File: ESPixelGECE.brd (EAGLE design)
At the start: 35.1 x 46 mm, 15 parts, among them Q1 MOSFET-NCHANNEL2N7000

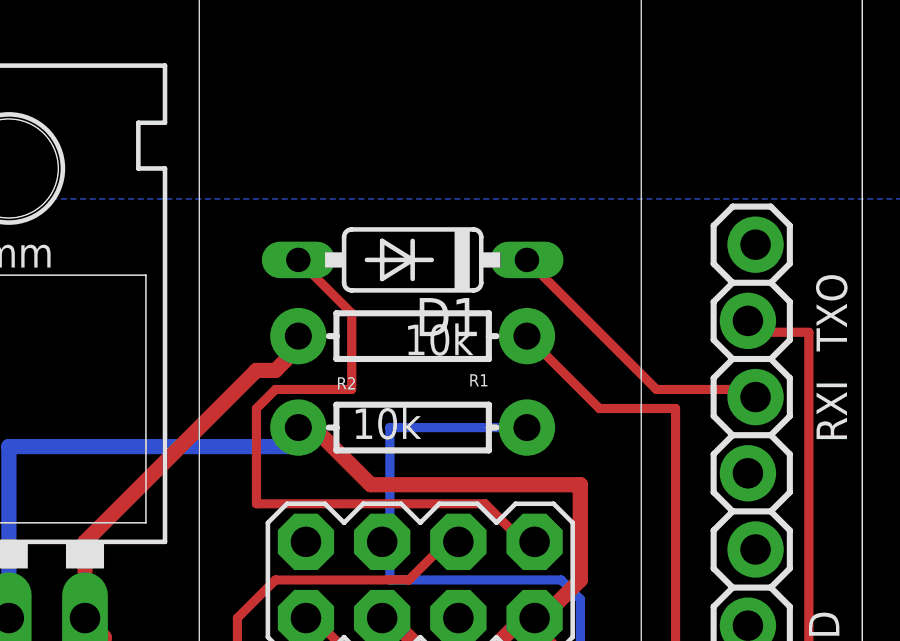
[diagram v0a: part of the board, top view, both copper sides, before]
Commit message: Added BOMs, SEEED cam
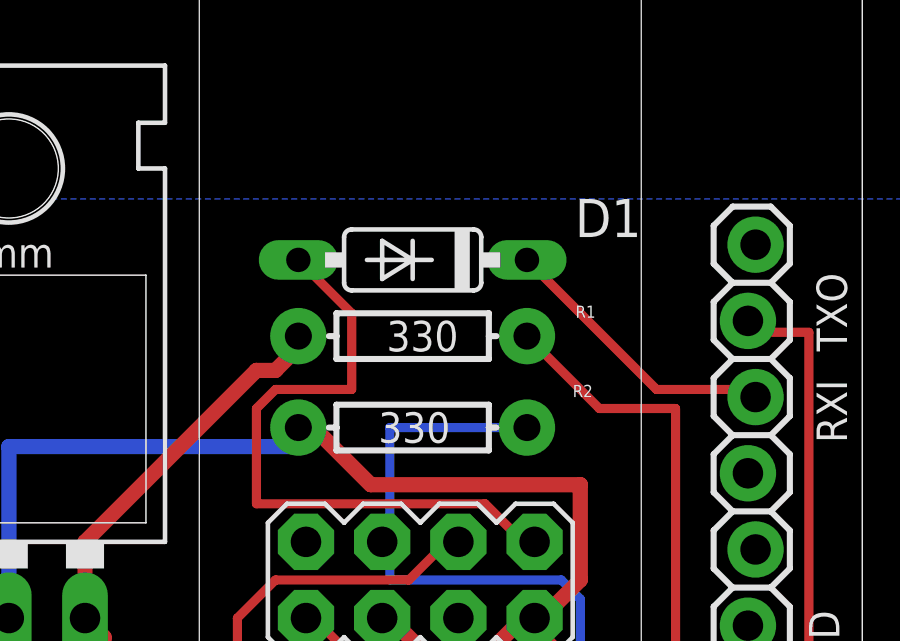
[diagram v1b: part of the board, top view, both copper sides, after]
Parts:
- R1, R2: value 10k -> 330
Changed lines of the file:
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@@
 <?xml version="1.0" encoding="utf-8"?>
 <!DOCTYPE eagle SYSTEM "eagle.dtd">
-<eagle version="7.2.0">
+<eagle version="7.4.0">
 <drawing>
 <settings>
@@
 </class>
 </classes>
-<designrules name="LaenPCBOrder">
+<designrules name="SeeedStudio_2layer_DRU_no_angle_20140221">
 <description language="de">&lt;b&gt;EAGLE Design Rules&lt;/b&gt;
 &lt;p&gt;
-Die Standard-Design-Rules sind so gewÃ¤hlt, dass sie fÃ¼r
+Die Standard-Design-Rules sind so gewählt, dass sie für
 die meisten Anwendungen passen. Sollte ihre Platine
 besondere Anforderungen haben, treffen Sie die erforderlichen
 Einstellungen hier und speichern die Design Rules unter
 einem neuen Namen ab.</description>
-<description language="en">&lt;b&gt;Laen's PCB Order Design Rules&lt;/b&gt;
+<description language="en">&lt;b&gt;EAGLE Design Rules&lt;/b&gt;
 &lt;p&gt;
-Please make sure your boards conform to these design rules.</description>
+The default Design Rules have been set to cover
+a wide range of applications. Your particular design
+may have different requirements, so please make the
+necessary adjustments and save your customized
+design rules under a new name.</description>
+<description language="zh">&lt;b&gt;Seeed Studio EAGLE Design Rules&lt;/b&gt;
+</description>
 <param name="layerSetup" value="(1*16)"/>
-<param name="mtCopper" value="0.0356mm 0.0356mm 0.0356mm 0.0356mm 0.0356mm 0.0356mm 0.0356mm 0.0356mm 0.0356mm 0.0356mm 0.0356mm 0.0356mm 0.0356mm 0.0356mm 0.0356mm 0.0356mm"/>
-<param name="mtIsolate" value="1.5011mm 0.1499mm 0.2007mm 0.1499mm 0.2007mm 0.1499mm 0.2007mm 0.1499mm 0.2007mm 0.1499mm 0.2007mm 0.1499mm 0.2007mm 0.1499mm 0.2007mm"/>
+<param name="mtCopper" value="0.035mm 0.0175mm 0.035mm 0.035mm 0.035mm 0.035mm 0.035mm 0.035mm 0.035mm 0.035mm 0.035mm 0.035mm 0.035mm 0.035mm 0.0175mm 0.035mm"/>
+<param name="mtIsolate" value="1.5mm 1.1mm 0.2mm 0.15mm 0.2mm 0.15mm 0.2mm 0.15mm 0.2mm 0.15mm 0.2mm 0.15mm 0.2mm 0.15mm 0.2mm"/>
 <param name="mdWireWire" value="6mil"/>
 <param name="mdWirePad" value="6mil"/>
@@
 <param name="mdPadVia" value="6mil"/>
 <param name="mdViaVia" value="6mil"/>
-<param name="mdSmdPad" value="6mil"/>
-<param name="mdSmdVia" value="6mil"/>
-<param name="mdSmdSmd" value="6mil"/>
+<param name="mdSmdPad" value="0mil"/>
+<param name="mdSmdVia" value="0mil"/>
+<param name="mdSmdSmd" value="0mil"/>
 <param name="mdViaViaSameLayer" value="8mil"/>
 <param name="mnLayersViaInSmd" value="2"/>
-<param name="mdCopperDimension" value="15mil"/>
-<param name="mdDrill" value="6mil"/>
+<param name="mdCopperDimension" value="10mil"/>
+<param name="mdDrill" value="10mil"/>
 <param name="mdSmdStop" value="0mil"/>
 <param name="msWidth" value="6mil"/>
-<param name="msDrill" value="13mil"/>
-<param name="msMicroVia" value="13mil"/>
+<param name="msDrill" value="12mil"/>
+<param name="msMicroVia" value="12mil"/>
 <param name="msBlindViaRatio" value="0.5"/>
 <param name="rvPadTop" value="0.25"/>
@@
 <param name="rvMicroViaOuter" value="0.25"/>
 <param name="rvMicroViaInner" value="0.25"/>
-<param name="rlMinPadTop" value="7mil"/>
+<param name="rlMinPadTop" value="10mil"/>
 <param name="rlMaxPadTop" value="20mil"/>
-<param name="rlMinPadInner" value="7mil"/>
+<param name="rlMinPadInner" value="10mil"/>
 <param name="rlMaxPadInner" value="20mil"/>
-<param name="rlMinPadBottom" value="7mil"/>
+<param name="rlMinPadBottom" value="10mil"/>
 <param name="rlMaxPadBottom" value="20mil"/>
-<param name="rlMinViaOuter" value="7mil"/>
+<param name="rlMinViaOuter" value="6mil"/>
 <param name="rlMaxViaOuter" value="20mil"/>
-<param name="rlMinViaInner" value="7mil"/>
+<param name="rlMinViaInner" value="6mil"/>
 <param name="rlMaxViaInner" value="20mil"/>
 <param name="rlMinMicroViaOuter" value="4mil"/>
@@
 <param name="psTop" value="-1"/>
 <param name="psBottom" value="-1"/>
-<param name="psFirst" value="-1"/>
+<param name="psFirst" value="0"/>
 <param name="psElongationLong" value="100"/>
 <param name="psElongationOffset" value="100"/>
 <param name="mvStopFrame" value="1"/>
 <param name="mvCreamFrame" value="0"/>
-<param name="mlMinStopFrame" value="3mil"/>
-<param name="mlMaxStopFrame" value="3mil"/>
+<param name="mlMinStopFrame" value="2mil"/>
+<param name="mlMaxStopFrame" value="2mil"/>
 <param name="mlMinCreamFrame" value="0mil"/>
 <param name="mlMaxCreamFrame" value="0mil"/>
-<param name="mlViaStopLimit" value="0mil"/>
+<param name="mlViaStopLimit" value="100mil"/>
 <param name="srRoundness" value="0"/>
 <param name="srMinRoundness" value="0mil"/>
@@
 <param name="checkAngle" value="0"/>
 <param name="checkFont" value="1"/>
-<param name="checkRestrict" value="1"/>
+<param name="checkRestrict" value="0"/>
 <param name="useDiameter" value="13"/>
 <param name="maxErrors" value="50"/>
@@
 <element name="U$2" library="SparkFun-Connectors" package="2X4" value="M04X2" x="41.656" y="27.94" smashed="yes"/>
 <element name="U$3" library="SparkFun-PowerIC" package="78XXL" value="V_REG_LD1117VXX" x="27.94" y="30.48" smashed="yes"/>
-<element name="R1" library="SparkFun-Resistors" package="AXIAL-0.3EZ" value="10k" x="41.402" y="36.068" rot="R180"/>
+<element name="R1" library="SparkFun-Resistors" package="AXIAL-0.3EZ" value="330" x="41.402" y="36.068" smashed="yes" rot="R180">
+<attribute name="NAME" x="47.498" y="37.084" size="0.4064" layer="25" font="vector" rot="R180"/>
+<attribute name="VALUE" x="42.926" y="36.576" size="1.016" layer="21" font="vector" ratio="15" rot="R180"/>
+</element>
 <element name="PAD1" library="wirepad" package="2.9/1.5" value="2.9/1.5" x="47.752" y="11.176" smashed="yes">
 <attribute name="VALUE" x="47.952" y="12.376" size="0.0254" layer="27"/>
@@
 <attribute name="NAME" x="51.943" y="22.225" size="0.4064" layer="25" ratio="10"/>
 </element>
-<element name="R2" library="SparkFun-Resistors" package="AXIAL-0.3EZ" value="10k" x="41.402" y="33.02"/>
-<element name="D1" library="diode" package="DO35-7" value="1N4148DO35-7" x="41.402" y="38.608" rot="R180"/>
+<element name="R2" library="SparkFun-Resistors" package="AXIAL-0.3EZ" value="330" x="41.402" y="33.02" smashed="yes">
+<attribute name="NAME" x="46.736" y="34.036" size="0.4064" layer="25" font="vector"/>
+<attribute name="VALUE" x="40.259" y="32.512" size="1.016" layer="21" font="vector" ratio="15"/>
+</element>
+<element name="D1" library="diode" package="DO35-7" value="1N4148DO35-7" x="41.402" y="38.608" smashed="yes" rot="R180">
+<attribute name="NAME" x="49.022" y="40.64" size="1.27" layer="25" ratio="10" rot="R180"/>
+</element>
 </elements>
 <signals>
